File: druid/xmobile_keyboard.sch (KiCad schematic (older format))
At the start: 34 parts

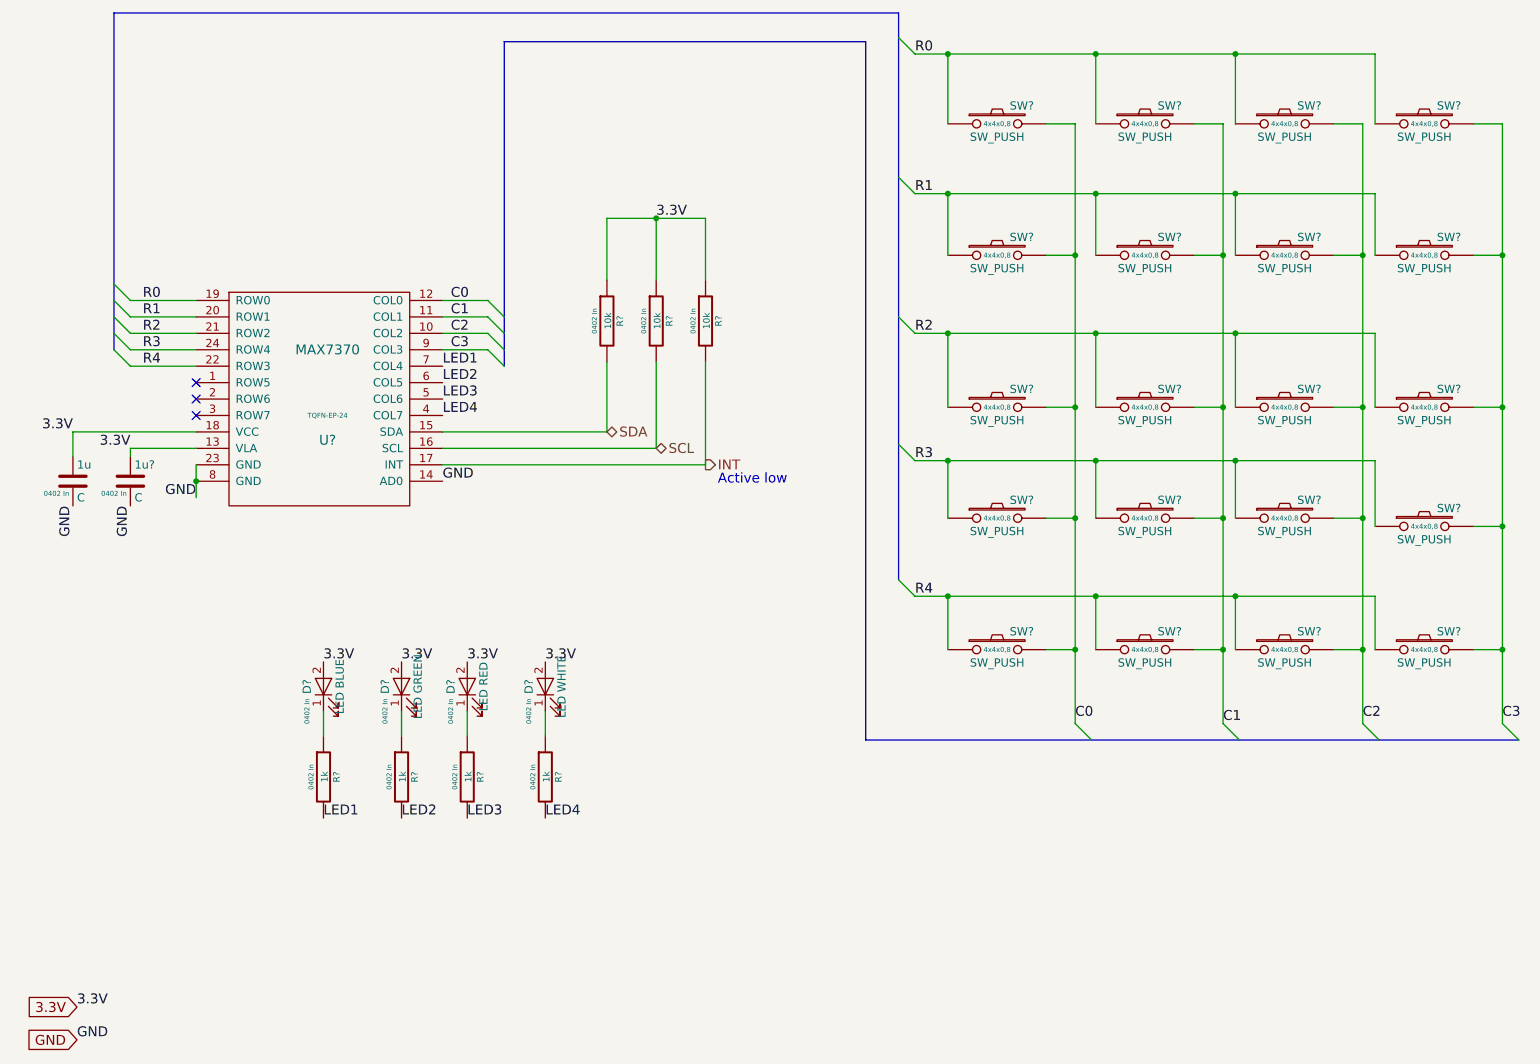
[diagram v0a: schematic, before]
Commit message: remove electric  warnings and errors. annotate elements. fix microUSB-B symbol.
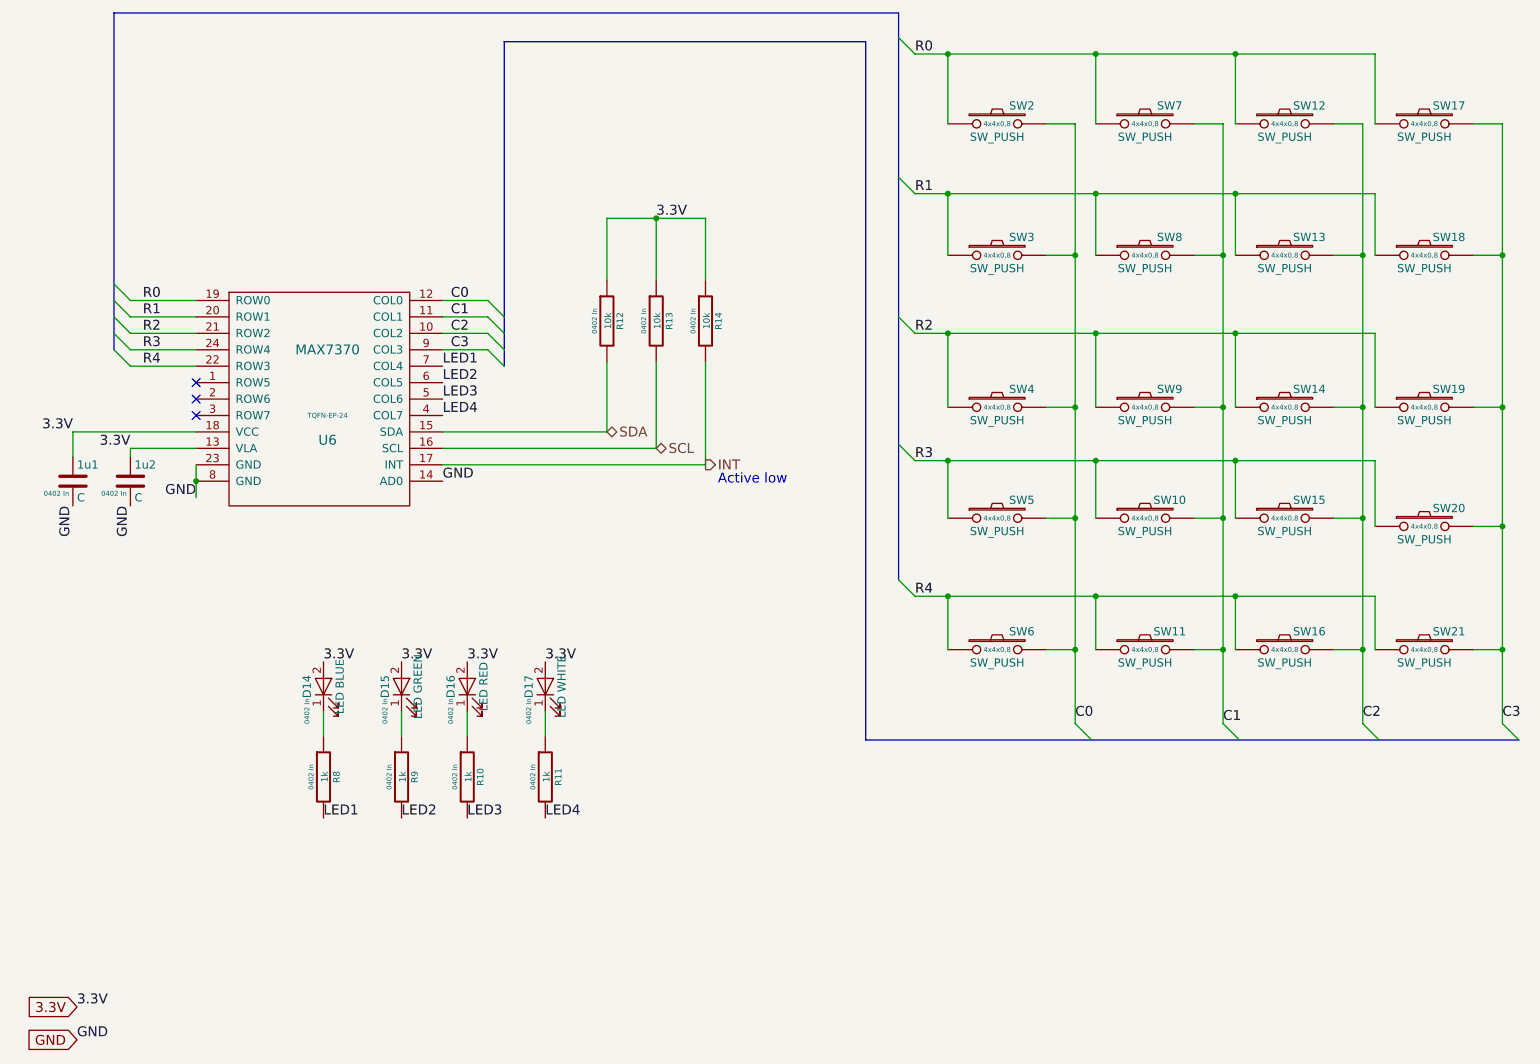
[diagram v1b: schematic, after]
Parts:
- gave numbers to parts that had none: 33
- renumbered 1u to 1u1
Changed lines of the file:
@@
 $EndDescr
 $Comp
-L xmobile-rescue:MAX7370 U?
+L xmobile-rescue:MAX7370 U6
 U 1 1 5C4B05E9
 P 2600 3750
-F 0 "U?" H 2600 3600 60  0000 C CNN
+F 0 "U6" H 2600 3600 60  0000 C CNN
 F 1 "MAX7370" H 2600 4150 60  0000 C CNN
 F 2 "druid:W252F2+1_21-0453" H 2575 3100 60  0001 C CNN
@@
 NoConn ~ 1800 3550
 $Comp
-L xmobile-rescue:R-RESCUE-xmobile R?
+L xmobile-rescue:R-RESCUE-xmobile R12
 U 1 1 5C49881F
 P 4300 3175
-F 0 "R?" V 4380 3175 40  0000 C CNN
+F 0 "R12" V 4380 3175 40  0000 C CNN
 F 1 "10k" V 4307 3176 40  0000 C CNN
 F 2 "Resistors_SMD:R_0402" V 4230 3175 30  0001 C CNN
@@
 INT
 $Comp
-L xmobile-rescue:C 1u
+L xmobile-rescue:C 1u1
 U 1 1 5C4C0F77
 P 1050 4150
-F 0 "1u" H 1075 4250 50  0000 L CNN
+F 0 "1u1" H 1075 4250 50  0000 L CNN
 F 1 "C" H 1075 4050 50  0000 L CNN
 F 2 "Capacitors_SMD:C_0402" H 1088 4000 50  0001 C CNN
@@
 Active low
 $Comp
-L xmobile-rescue:LED-RESCUE-xmobile D?
+L xmobile-rescue:LED-RESCUE-xmobile D14
 U 1 1 5C4C2FCD
 P 2575 5400
-F 0 "D?" H 2575 5500 50  0000 C CNN
+F 0 "D14" H 2575 5500 50  0000 C CNN
 F 1 "LED BLUE" H 2575 5300 50  0000 C CNN
 F 2 "LEDs_git:LED_0402" H 2575 5400 50  0001 C CNN
@@
 3.3V
 $Comp
-L xmobile-rescue:R-RESCUE-xmobile R?
+L xmobile-rescue:R-RESCUE-xmobile R8
 U 1 1 5C4C321E
 P 2575 5950
-F 0 "R?" V 2655 5950 40  0000 C CNN
+F 0 "R8" V 2655 5950 40  0000 C CNN
 F 1 "1k" V 2582 5951 40  0000 C CNN
 F 2 "Resistors_SMD:R_0402" V 2505 5950 30  0001 C CNN
@@
 	2575 5550 2575 5700
 $Comp
-L xmobile-rescue:LED-RESCUE-xmobile D?
+L xmobile-rescue:LED-RESCUE-xmobile D15
 U 1 1 5C4C4192
 P 3050 5400
-F 0 "D?" H 3050 5500 50  0000 C CNN
+F 0 "D15" H 3050 5500 50  0000 C CNN
 F 1 "LED GREEN" H 3050 5300 50  0000 C CNN
 F 2 "LEDs_git:LED_0402" H 3050 5400 50  0001 C CNN
@@
 	3050 5550 3050 5700
 $Comp
-L xmobile-rescue:LED-RESCUE-xmobile D?
+L xmobile-rescue:LED-RESCUE-xmobile D16
 U 1 1 5C4C43FA
 P 3450 5400
-F 0 "D?" H 3450 5500 50  0000 C CNN
+F 0 "D16" H 3450 5500 50  0000 C CNN
 F 1 "LED RED" H 3450 5300 50  0000 C CNN
 F 2 "LEDs_git:LED_0402" H 3450 5400 50  0001 C CNN
@@
 	3450 5550 3450 5700
 $Comp
-L xmobile-rescue:LED-RESCUE-xmobile D?
+L xmobile-rescue:LED-RESCUE-xmobile D17
 U 1 1 5C4C4408
 P 3925 5400
-F 0 "D?" H 3925 5500 50  0000 C CNN
+F 0 "D17" H 3925 5500 50  0000 C CNN
 F 1 "LED WHITE" H 3925 5300 50  0000 C CNN
 F 2 "LEDs_git:LED_0402" H 3925 5400 50  0001 C CNN
@@
 LED4
 $Comp
-L xmobile-rescue:SW_PUSH SW?
+L xmobile-rescue:SW_PUSH SW2
 U 1 1 5C4FFA32
 P 6675 1975
-F 0 "SW?" H 6825 2085 50  0000 C CNN
+F 0 "SW2" H 6825 2085 50  0000 C CNN
 F 1 "SW_PUSH" H 6675 1895 50  0000 C CNN
 F 2 "druid:button_4pin_7,5x5" H 6675 2175 50  0001 C CNN
@@
 	9750 1975 9750 2775
 $Comp
-L xmobile-rescue:SW_PUSH SW?
+L xmobile-rescue:SW_PUSH SW7
 U 1 1 5C6DCE7B
 P 7575 1975
-F 0 "SW?" H 7725 2085 50  0000 C CNN
+F 0 "SW7" H 7725 2085 50  0000 C CNN
 F 1 "SW_PUSH" H 7575 1895 50  0000 C CNN
 F 2 "druid:button_4pin_7,5x5" H 7575 2175 50  0001 C CNN
@@
 $EndComp
 $Comp
-L xmobile-rescue:SW_PUSH SW?
+L xmobile-rescue:SW_PUSH SW12
 U 1 1 5C6DCF38
 P 8425 1975
-F 0 "SW?" H 8575 2085 50  0000 C CNN
+F 0 "SW12" H 8575 2085 50  0000 C CNN
 F 1 "SW_PUSH" H 8425 1895 50  0000 C CNN
 F 2 "druid:button_4pin_7,5x5" H 8425 2175 50  0001 C CNN
@@
 $EndComp
 $Comp
-L xmobile-rescue:SW_PUSH SW?
+L xmobile-rescue:SW_PUSH SW3
 U 1 1 5C6DD084
 P 6675 2775
-F 0 "SW?" H 6825 2885 50  0000 C CNN
+F 0 "SW3" H 6825 2885 50  0000 C CNN
 F 1 "SW_PUSH" H 6675 2695 50  0000 C CNN
 F 2 "druid:button_4pin_7,5x5" H 6675 2975 50  0001 C CNN
@@
 $EndComp
 $Comp
-L xmobile-rescue:SW_PUSH SW?
+L xmobile-rescue:SW_PUSH SW8
 U 1 1 5C6DD126
 P 7575 2775
-F 0 "SW?" H 7725 2885 50  0000 C CNN
+F 0 "SW8" H 7725 2885 50  0000 C CNN
 F 1 "SW_PUSH" H 7575 2695 50  0000 C CNN
 F 2 "druid:button_4pin_7,5x5" H 7575 2975 50  0001 C CNN
@@
 $EndComp
 $Comp
-L xmobile-rescue:SW_PUSH SW?
+L xmobile-rescue:SW_PUSH SW13
 U 1 1 5C6DD1D1
 P 8425 2775
-F 0 "SW?" H 8575 2885 50  0000 C CNN
+F 0 "SW13" H 8575 2885 50  0000 C CNN
 F 1 "SW_PUSH" H 8425 2695 50  0000 C CNN
 F 2 "druid:button_4pin_7,5x5" H 8425 2975 50  0001 C CNN
@@
 $EndComp
 $Comp
-L xmobile-rescue:SW_PUSH SW?
+L xmobile-rescue:SW_PUSH SW17
 U 1 1 5C6DD300
 P 9275 1975
-F 0 "SW?" H 9425 2085 50  0000 C CNN
+F 0 "SW17" H 9425 2085 50  0000 C CNN
 F 1 "SW_PUSH" H 9275 1895 50  0000 C CNN
 F 2 "druid:button_4pin_7,5x5" H 9275 2175 50  0001 C CNN
@@
 $EndComp
 $Comp
-L xmobile-rescue:SW_PUSH SW?
+L xmobile-rescue:SW_PUSH SW18
 U 1 1 5C6DD3BD
 P 9275 2775
-F 0 "SW?" H 9425 2885 50  0000 C CNN
+F 0 "SW18" H 9425 2885 50  0000 C CNN
 F 1 "SW_PUSH" H 9275 2695 50  0000 C CNN
 F 2 "druid:button_4pin_7,5x5" H 9275 2975 50  0001 C CNN
@@
 $EndComp
 $Comp
-L xmobile-rescue:SW_PUSH SW?
+L xmobile-rescue:SW_PUSH SW4
 U 1 1 5C6DD583
 P 6675 3700
-F 0 "SW?" H 6825 3810 50  0000 C CNN
+F 0 "SW4" H 6825 3810 50  0000 C CNN
 F 1 "SW_PUSH" H 6675 3620 50  0000 C CNN
 F 2 "druid:button_4pin_7,5x5" H 6675 3900 50  0001 C CNN
@@
 $EndComp
 $Comp
-L xmobile-rescue:SW_PUSH SW?
+L xmobile-rescue:SW_PUSH SW5
 U 1 1 5C6DD636
 P 6675 4375
-F 0 "SW?" H 6825 4485 50  0000 C CNN
+F 0 "SW5" H 6825 4485 50  0000 C CNN
 F 1 "SW_PUSH" H 6675 4295 50  0000 C CNN
 F 2 "druid:button_4pin_7,5x5" H 6675 4575 50  0001 C CNN
@@
 $EndComp
 $Comp
-L xmobile-rescue:SW_PUSH SW?
+L xmobile-rescue:SW_PUSH SW10
 U 1 1 5C6DD6E4
 P 7575 4375
-F 0 "SW?" H 7725 4485 50  0000 C CNN
+F 0 "SW10" H 7725 4485 50  0000 C CNN
 F 1 "SW_PUSH" H 7575 4295 50  0000 C CNN
 F 2 "druid:button_4pin_7,5x5" H 7575 4575 50  0001 C CNN
@@
 $EndComp
 $Comp
-L xmobile-rescue:SW_PUSH SW?
+L xmobile-rescue:SW_PUSH SW9
 U 1 1 5C6DD787
 P 7575 3700
-F 0 "SW?" H 7725 3810 50  0000 C CNN
+F 0 "SW9" H 7725 3810 50  0000 C CNN
 F 1 "SW_PUSH" H 7575 3620 50  0000 C CNN
 F 2 "druid:button_4pin_7,5x5" H 7575 3900 50  0001 C CNN
@@
 $EndComp
 $Comp
-L xmobile-rescue:SW_PUSH SW?
+L xmobile-rescue:SW_PUSH SW14
 U 1 1 5C6DD88C
 P 8425 3700
-F 0 "SW?" H 8575 3810 50  0000 C CNN
+F 0 "SW14" H 8575 3810 50  0000 C CNN
 F 1 "SW_PUSH" H 8425 3620 50  0000 C CNN
 F 2 "druid:button_4pin_7,5x5" H 8425 3900 50  0001 C CNN
@@
 $EndComp
 $Comp
-L xmobile-rescue:SW_PUSH SW?
+L xmobile-rescue:SW_PUSH SW15
 U 1 1 5C6DD941
 P 8425 4375
-F 0 "SW?" H 8575 4485 50  0000 C CNN
+F 0 "SW15" H 8575 4485 50  0000 C CNN
 F 1 "SW_PUSH" H 8425 4295 50  0000 C CNN
 F 2 "druid:button_4pin_7,5x5" H 8425 4575 50  0001 C CNN
@@
 $EndComp
 $Comp
-L xmobile-rescue:SW_PUSH SW?
+L xmobile-rescue:SW_PUSH SW19
 U 1 1 5C6DDA70
 P 9275 3700
-F 0 "SW?" H 9425 3810 50  0000 C CNN
+F 0 "SW19" H 9425 3810 50  0000 C CNN
 F 1 "SW_PUSH" H 9275 3620 50  0000 C CNN
 F 2 "druid:button_4pin_7,5x5" H 9275 3900 50  0001 C CNN
@@
 $EndComp
 $Comp
-L xmobile-rescue:SW_PUSH SW?
+L xmobile-rescue:SW_PUSH SW20
 U 1 1 5C6DDB57
 P 9275 4425
-F 0 "SW?" H 9425 4535 50  0000 C CNN
+F 0 "SW20" H 9425 4535 50  0000 C CNN
 F 1 "SW_PUSH" H 9275 4345 50  0000 C CNN
 F 2 "druid:button_4pin_7,5x5" H 9275 4625 50  0001 C CNN
@@
 $EndComp
 $Comp
-L xmobile-rescue:SW_PUSH SW?
+L xmobile-rescue:SW_PUSH SW6
 U 1 1 5C6DDCFE
 P 6675 5175
-F 0 "SW?" H 6825 5285 50  0000 C CNN
+F 0 "SW6" H 6825 5285 50  0000 C CNN
 F 1 "SW_PUSH" H 6675 5095 50  0000 C CNN
 F 2 "druid:button_4pin_7,5x5" H 6675 5375 50  0001 C CNN
@@
 $EndComp
 $Comp
-L xmobile-rescue:SW_PUSH SW?
+L xmobile-rescue:SW_PUSH SW11
 U 1 1 5C6DDDAF
 P 7575 5175
-F 0 "SW?" H 7725 5285 50  0000 C CNN
+F 0 "SW11" H 7725 5285 50  0000 C CNN
 F 1 "SW_PUSH" H 7575 5095 50  0000 C CNN
 F 2 "druid:button_4pin_7,5x5" H 7575 5375 50  0001 C CNN
@@
 $EndComp
 $Comp
-L xmobile-rescue:SW_PUSH SW?
+L xmobile-rescue:SW_PUSH SW16
 U 1 1 5C6DDEF8
 P 8425 5175
-F 0 "SW?" H 8575 5285 50  0000 C CNN
+F 0 "SW16" H 8575 5285 50  0000 C CNN
 F 1 "SW_PUSH" H 8425 5095 50  0000 C CNN
 F 2 "druid:button_4pin_7,5x5" H 8425 5375 50  0001 C CNN
@@
 $EndComp
 $Comp
-L xmobile-rescue:SW_PUSH SW?
+L xmobile-rescue:SW_PUSH SW21
 U 1 1 5C6DDFAF
 P 9275 5175
-F 0 "SW?" H 9425 5285 50  0000 C CNN
+F 0 "SW21" H 9425 5285 50  0000 C CNN
 F 1 "SW_PUSH" H 9275 5095 50  0000 C CNN
 F 2 "druid:button_4pin_7,5x5" H 9275 5375 50  0001 C CNN
@@
 $EndComp
 $Comp
-L xmobile-rescue:C 1u?
+L xmobile-rescue:C 1u2
 U 1 1 5C6E6190
 P 1400 4150
-F 0 "1u?" H 1425 4250 50  0000 L CNN
+F 0 "1u2" H 1425 4250 50  0000 L CNN
 F 1 "C" H 1425 4050 50  0000 L CNN
 F 2 "Capacitors_SMD:C_0402" H 1438 4000 50  0001 C CNN
@@
 $EndComp
 $Comp
-L xmobile-rescue:R-RESCUE-xmobile R?
+L xmobile-rescue:R-RESCUE-xmobile R9
 U 1 1 5C6E6DE1
 P 3050 5950
-F 0 "R?" V 3130 5950 40  0000 C CNN
+F 0 "R9" V 3130 5950 40  0000 C CNN
 F 1 "1k" V 3057 5951 40  0000 C CNN
 F 2 "Resistors_SMD:R_0402" V 2980 5950 30  0001 C CNN
@@
 $EndComp
 $Comp
-L xmobile-rescue:R-RESCUE-xmobile R?
+L xmobile-rescue:R-RESCUE-xmobile R10
 U 1 1 5C6E6E9E
 P 3450 5950
-F 0 "R?" V 3530 5950 40  0000 C CNN
+F 0 "R10" V 3530 5950 40  0000 C CNN
 F 1 "1k" V 3457 5951 40  0000 C CNN
 F 2 "Resistors_SMD:R_0402" V 3380 5950 30  0001 C CNN
@@
 $EndComp
 $Comp
-L xmobile-rescue:R-RESCUE-xmobile R?
+L xmobile-rescue:R-RESCUE-xmobile R13
 U 1 1 5C6E7B9A
 P 4600 3175
-F 0 "R?" V 4680 3175 40  0000 C CNN
+F 0 "R13" V 4680 3175 40  0000 C CNN
 F 1 "10k" V 4607 3176 40  0000 C CNN
 F 2 "Resistors_SMD:R_0402" V 4530 3175 30  0001 C CNN
@@
 $EndComp
 $Comp
-L xmobile-rescue:R-RESCUE-xmobile R?
+L xmobile-rescue:R-RESCUE-xmobile R14
 U 1 1 5C6E7C9E
 P 4900 3175
-F 0 "R?" V 4980 3175 40  0000 C CNN
+F 0 "R14" V 4980 3175 40  0000 C CNN
 F 1 "10k" V 4907 3176 40  0000 C CNN
 F 2 "Resistors_SMD:R_0402" V 4830 3175 30  0001 C CNN
@@
 $EndComp
 $Comp
-L xmobile-rescue:R-RESCUE-xmobile R?
+L xmobile-rescue:R-RESCUE-xmobile R11
 U 1 1 5C6E62AB
 P 3925 5950
-F 0 "R?" V 4005 5950 40  0000 C CNN
+F 0 "R11" V 4005 5950 40  0000 C CNN
 F 1 "1k" V 3932 5951 40  0000 C CNN
 F 2 "Resistors_SMD:R_0402" V 3855 5950 30  0001 C CNN

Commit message: fix other packages. Start doing layout
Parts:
- 1u1, 1u2: footprint Capacitors_SMD:C_0402 -> Capacitor_SMD:C_0402_1005Metric
- D14, D15, D16, D17: footprint LEDs_git:LED_0402 -> LED_SMD:LED_0402_1005Metric
- R10, R11, R12, R13, R14, R8, R9: footprint Resistors_SMD:R_0402 -> Resistor_SMD:R_0402_1005Metric
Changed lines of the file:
@@
 F 0 "R12" V 4380 3175 40  0000 C CNN
 F 1 "10k" V 4307 3176 40  0000 C CNN
-F 2 "Resistors_SMD:R_0402" V 4230 3175 30  0001 C CNN
+F 2 "Resistor_SMD:R_0402_1005Metric" V 4230 3175 30  0001 C CNN
 F 3 "https://eu.mouser.com/datasheet/2/348/sfr-e-1507454.pdf" H 4300 3175 30  0001 C CNN
 F 4 "https://eu.mouser.com/ProductDetail/ROHM-Semiconductor/SFR01MZPJ103?qs=sGAEpiMZZMtlubZbdhIBIIR71ikvQRXLchgEzboAcvI%3d" V 4300 3175 60  0001 C CNN "example"
@@
 F 0 "1u1" H 1075 4250 50  0000 L CNN
 F 1 "C" H 1075 4050 50  0000 L CNN
-F 2 "Capacitors_SMD:C_0402" H 1088 4000 50  0001 C CNN
+F 2 "Capacitor_SMD:C_0402_1005Metric" H 1088 4000 50  0001 C CNN
 F 3 "https://eu.mouser.com/datasheet/2/281/murata_03052018_GRM_Series_1-1310166.pdf" H 1050 4150 50  0001 C CNN
 F 4 "close to chip" H 1050 4150 60  0001 C CNN "note"
@@
 F 0 "D14" H 2575 5500 50  0000 C CNN
 F 1 "LED BLUE" H 2575 5300 50  0000 C CNN
-F 2 "LEDs_git:LED_0402" H 2575 5400 50  0001 C CNN
+F 2 "LED_SMD:LED_0402_1005Metric" H 2575 5400 50  0001 C CNN
 F 3 "https://eu.mouser.com/datasheet/2/348/sml-p1-e-1139198.pdf" H 2575 5400 50  0001 C CNN
 F 4 "https://eu.mouser.com/ProductDetail/ROHM-Semiconductor/SMLP13BC8TT86?qs=sGAEpiMZZMuCm2JlHBGefhkTP7nu0Fg7%2fyfWOmjl5dYVsL3Njh32dw%3d%3d" H 2575 5400 60  0001 C CNN "example"
@@
 F 0 "R8" V 2655 5950 40  0000 C CNN
 F 1 "1k" V 2582 5951 40  0000 C CNN
-F 2 "Resistors_SMD:R_0402" V 2505 5950 30  0001 C CNN
+F 2 "Resistor_SMD:R_0402_1005Metric" V 2505 5950 30  0001 C CNN
 F 3 "https://eu.mouser.com/datasheet/2/427/crcwce3-1223726.pdf" H 2575 5950 30  0001 C CNN
 F 4 "https://eu.mouser.com/ProductDetail/Vishay/CRCW04021K00FKEDC?qs=sGAEpiMZZMtlubZbdhIBIIZe04wfiaJWtbhT4BxhiTc%3d" V 2575 5950 60  0001 C CNN "example"
@@
 F 0 "D15" H 3050 5500 50  0000 C CNN
 F 1 "LED GREEN" H 3050 5300 50  0000 C CNN
-F 2 "LEDs_git:LED_0402" H 3050 5400 50  0001 C CNN
+F 2 "LED_SMD:LED_0402_1005Metric" H 3050 5400 50  0001 C CNN
 F 3 "https://eu.mouser.com/datasheet/2/348/sml-p1-e-1139198.pdf" H 3050 5400 50  0001 C CNN
 F 4 "https://eu.mouser.com/ProductDetail/ROHM-Semiconductor/SML-P13PTT86R?qs=sGAEpiMZZMuCm2JlHBGefsrOrFaWoqzN4Th3QTRUboF5qJIQuUKd%2fg%3d%3d" H 3050 5400 60  0001 C CNN "example"
@@
 F 0 "D16" H 3450 5500 50  0000 C CNN
 F 1 "LED RED" H 3450 5300 50  0000 C CNN
-F 2 "LEDs_git:LED_0402" H 3450 5400 50  0001 C CNN
+F 2 "LED_SMD:LED_0402_1005Metric" H 3450 5400 50  0001 C CNN
 F 3 "https://eu.mouser.com/datasheet/2/348/sml-p1-e-1139198.pdf" H 3450 5400 50  0001 C CNN
 F 4 "https://eu.mouser.com/ProductDetail/ROHM-Semiconductor/SML-P12U2TT86R?qs=sGAEpiMZZMuCm2JlHBGefsrOrFaWoqzNOGPWK3jFzCB54s8pBFBg3g%3d%3d" H 3450 5400 60  0001 C CNN "example"
@@
 F 0 "D17" H 3925 5500 50  0000 C CNN
 F 1 "LED WHITE" H 3925 5300 50  0000 C CNN
-F 2 "LEDs_git:LED_0402" H 3925 5400 50  0001 C CNN
+F 2 "LED_SMD:LED_0402_1005Metric" H 3925 5400 50  0001 C CNN
 F 3 "https://media.osram.info/media/resource/hires/osram-dam-2493126/LW%20QH8G.pdf" H 3925 5400 50  0001 C CNN
 F 4 "https://eu.mouser.com/ProductDetail/OSRAM-Opto-Semiconductors/LW-QH8G-Q2OO-3K5L?qs=sGAEpiMZZMuCm2JlHBGefutc4sI%252bRg9%2fGvzrBju18VEuEONgNlSGyQ%3d%3d" H 3925 5400 60  0001 C CNN "example"
@@
 F 0 "1u2" H 1425 4250 50  0000 L CNN
 F 1 "C" H 1425 4050 50  0000 L CNN
-F 2 "Capacitors_SMD:C_0402" H 1438 4000 50  0001 C CNN
+F 2 "Capacitor_SMD:C_0402_1005Metric" H 1438 4000 50  0001 C CNN
 F 3 "https://eu.mouser.com/datasheet/2/281/murata_03052018_GRM_Series_1-1310166.pdf" H 1400 4150 50  0001 C CNN
 F 4 "close to chip" H 1400 4150 60  0001 C CNN "note"
@@
 F 0 "R9" V 3130 5950 40  0000 C CNN
 F 1 "1k" V 3057 5951 40  0000 C CNN
-F 2 "Resistors_SMD:R_0402" V 2980 5950 30  0001 C CNN
+F 2 "Resistor_SMD:R_0402_1005Metric" V 2980 5950 30  0001 C CNN
 F 3 "https://eu.mouser.com/datasheet/2/427/crcwce3-1223726.pdf" H 3050 5950 30  0001 C CNN
 F 4 "https://eu.mouser.com/ProductDetail/Vishay/CRCW04021K00FKEDC?qs=sGAEpiMZZMtlubZbdhIBIIZe04wfiaJWtbhT4BxhiTc%3d" V 3050 5950 60  0001 C CNN "example"
@@
 F 0 "R10" V 3530 5950 40  0000 C CNN
 F 1 "1k" V 3457 5951 40  0000 C CNN
-F 2 "Resistors_SMD:R_0402" V 3380 5950 30  0001 C CNN
+F 2 "Resistor_SMD:R_0402_1005Metric" V 3380 5950 30  0001 C CNN
 F 3 "https://eu.mouser.com/datasheet/2/427/crcwce3-1223726.pdf" H 3450 5950 30  0001 C CNN
 F 4 "https://eu.mouser.com/ProductDetail/Vishay/CRCW04021K00FKEDC?qs=sGAEpiMZZMtlubZbdhIBIIZe04wfiaJWtbhT4BxhiTc%3d" V 3450 5950 60  0001 C CNN "example"
@@
 F 0 "R13" V 4680 3175 40  0000 C CNN
 F 1 "10k" V 4607 3176 40  0000 C CNN
-F 2 "Resistors_SMD:R_0402" V 4530 3175 30  0001 C CNN
+F 2 "Resistor_SMD:R_0402_1005Metric" V 4530 3175 30  0001 C CNN
 F 3 "https://eu.mouser.com/datasheet/2/348/sfr-e-1507454.pdf" H 4600 3175 30  0001 C CNN
 F 4 "https://eu.mouser.com/ProductDetail/ROHM-Semiconductor/SFR01MZPJ103?qs=sGAEpiMZZMtlubZbdhIBIIR71ikvQRXLchgEzboAcvI%3d" V 4600 3175 60  0001 C CNN "example"
@@
 F 0 "R14" V 4980 3175 40  0000 C CNN
 F 1 "10k" V 4907 3176 40  0000 C CNN
-F 2 "Resistors_SMD:R_0402" V 4830 3175 30  0001 C CNN
+F 2 "Resistor_SMD:R_0402_1005Metric" V 4830 3175 30  0001 C CNN
 F 3 "https://eu.mouser.com/datasheet/2/348/sfr-e-1507454.pdf" H 4900 3175 30  0001 C CNN
 F 4 "https://eu.mouser.com/ProductDetail/ROHM-Semiconductor/SFR01MZPJ103?qs=sGAEpiMZZMtlubZbdhIBIIR71ikvQRXLchgEzboAcvI%3d" V 4900 3175 60  0001 C CNN "example"
@@
 F 0 "R11" V 4005 5950 40  0000 C CNN
 F 1 "1k" V 3932 5951 40  0000 C CNN
-F 2 "Resistors_SMD:R_0402" V 3855 5950 30  0001 C CNN
+F 2 "Resistor_SMD:R_0402_1005Metric" V 3855 5950 30  0001 C CNN
 F 3 "https://eu.mouser.com/datasheet/2/427/crcwce3-1223726.pdf" H 3925 5950 30  0001 C CNN
 F 4 "https://eu.mouser.com/ProductDetail/Vishay/CRCW04021K00FKEDC?qs=sGAEpiMZZMtlubZbdhIBIIZe04wfiaJWtbhT4BxhiTc%3d" V 3925 5950 60  0001 C CNN "example"
